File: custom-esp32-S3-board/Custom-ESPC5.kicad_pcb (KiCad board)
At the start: 4 copper layers, 63.5 x 57.1 mm, 43 parts, among them J1 Screw_Terminal_01x02, J10 Barrel_Jack, J12 Conn_01x05, J13 Conn_01x05, J4 USB_C_Receptacle_USB2.0_14P, J5 Conn_01x03, J6 Screw_Terminal_01x03, SW1 SW_Nidec_CAS-120A1, SW2 SW_Push, SW3 SW_Push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

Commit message: Update layout
apply schematic changes to layout
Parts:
- added C10: 10µF, Capacitor_SMD:C_0402_1005Metric, F.Cu at (117.5, 94.0)
- added C11: 0.1uF, Capacitor_SMD:C_0402_1005Metric, F.Cu at (117.5, 96.0)
- added C12: 0.1µF, Capacitor_SMD:C_0402_1005Metric, F.Cu at (117.5, 97.9)
- added C13: 0.1µF, Capacitor_SMD:C_0402_1005Metric, F.Cu at (117.5, 99.9)
- added C15: 10µF, Capacitor_SMD:C_0402_1005Metric, F.Cu at (117.5, 101.9)
- added C16: 0.1µF, Capacitor_SMD:C_0402_1005Metric, F.Cu at (117.5, 103.8)
- added C9: 0.1uF, Capacitor_SMD:C_0402_1005Metric, F.Cu at (117.5, 92.0)
- added R10: 3.3k, Resistor_SMD:R_0402_1005Metric, F.Cu at (120.4, 92.0)
- added R12: 3.3k, Resistor_SMD:R_0402_1005Metric, F.Cu at (120.4, 94.0)
- R1: value 910 -> 750
- U2: value LM317DCYR -> LM317KCS; footprint Package_TO_SOT_SMD:SOT-223-3_TabPin2 -> Package_TO_SOT_THT:TO-220-3_Vertical
- U4: value LM3940 -> LM3940IT-3.3; footprint Package_TO_SOT_SMD:SOT-223-3_TabPin2 -> Package_TO_SOT_THT:TO-220-3_Vertical
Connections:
- U3 pad 6: +3.3V -> CP2102_VDD

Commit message: Fix pin labels in schematic
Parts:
- removed D1, D4: D, Diode_SMD:USC-TOS
- added C17: 0.1u, Capacitor_SMD:C_0402_1005Metric, F.Cu at (125.9, 111.2)
- added C18: 0.1u, Capacitor_SMD:C_0402_1005Metric, F.Cu at (125.9, 113.2)
- added C19: 0.1u, Capacitor_SMD:C_0402_1005Metric, F.Cu at (125.9, 115.1)
- added C20: 0.1u, Capacitor_SMD:C_0402_1005Metric, F.Cu at (125.9, 117.1)
- added J2: Conn_01x02_Pin, Connector_PinHeader_2.54mm:PinHeader_1x02_P2.54mm_Vertical, F.Cu at (126.8, 105.4)
- added J3: Conn_01x02_Pin, Connector_PinHeader_2.54mm:PinHeader_1x02_P2.54mm_Vertical, F.Cu at (131.4, 105.4)
- added J7: Conn_01x02_Pin, Connector_PinHeader_2.54mm:PinHeader_1x02_P2.54mm_Vertical, F.Cu at (136.0, 105.4)
- added J8: Conn_01x02_Pin, Connector_PinHeader_2.54mm:PinHeader_1x02_P2.54mm_Vertical, F.Cu at (140.6, 105.4)
- added Q1: BC847BDW1, Package_TO_SOT_SMD:SOT-363_SC-70-6, F.Cu at (129.7, 112.1)
- added R13: 10k, Resistor_SMD:R_0402_1005Metric, F.Cu at (128.8, 114.8)
- added R14: 10k, Resistor_SMD:R_0402_1005Metric, F.Cu at (128.8, 116.8)
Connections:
- net /UART RX renamed /UART0 RX
- net /UART TX renamed /UART0 TX
- J5 pad 1: +3.3V -> /UART1_TX
- J5 pad 2: /WS2812 -> /UART1_RX
- U6 pad 10: /WS2812 -> /UART1 TX
- U6 pad 11: unconnected-(U6-IO18-Pad11) -> /UART1 RX
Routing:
- net (no net): track 0.00 -> 137.0 mm, vias 0 -> 1
- net /WS2812: track 51.5 -> 0.00 mm, vias 1 -> 0
- net /UART0 RX: track 34.7 -> 0.00 mm
- net /UART0 TX: track 33.7 -> 0.00 mm
- net Net-(J8-Pin_1): track 17.0 -> 0.00 mm

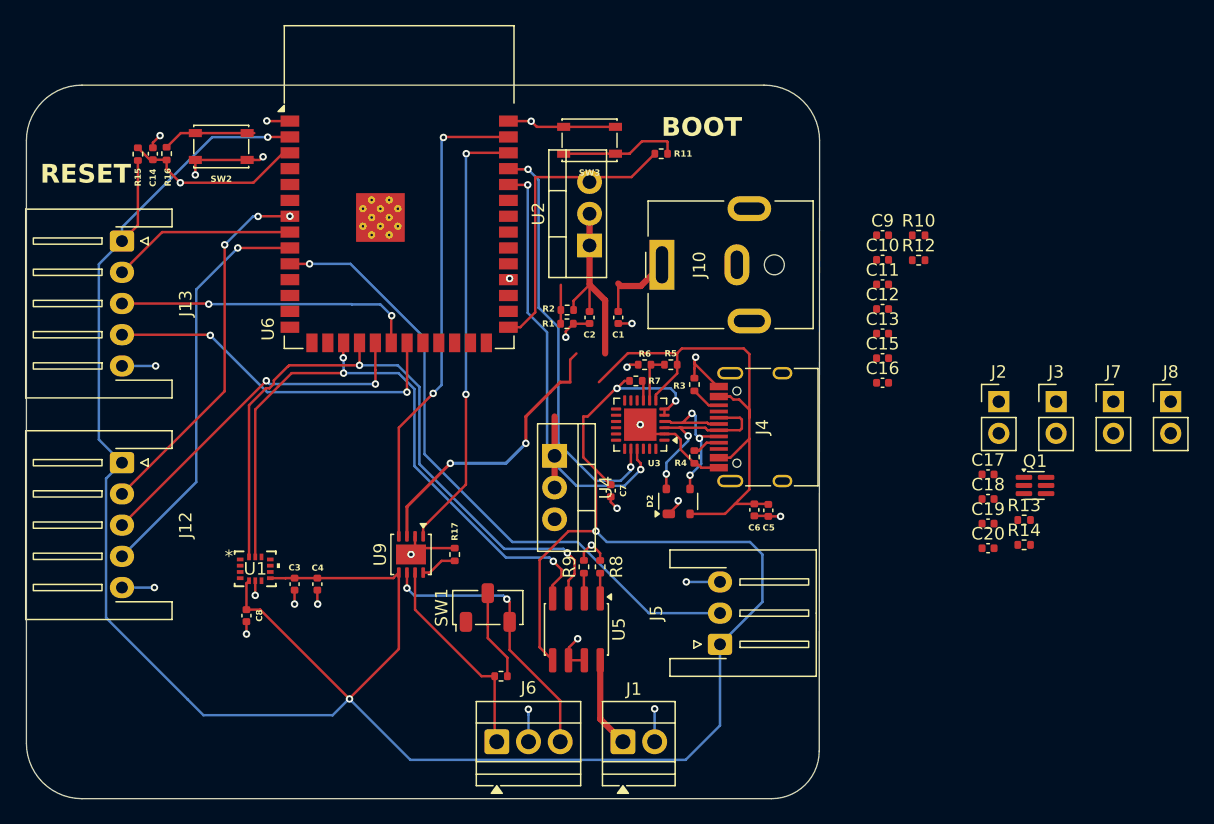
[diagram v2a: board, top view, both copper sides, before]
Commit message: Place components for layout
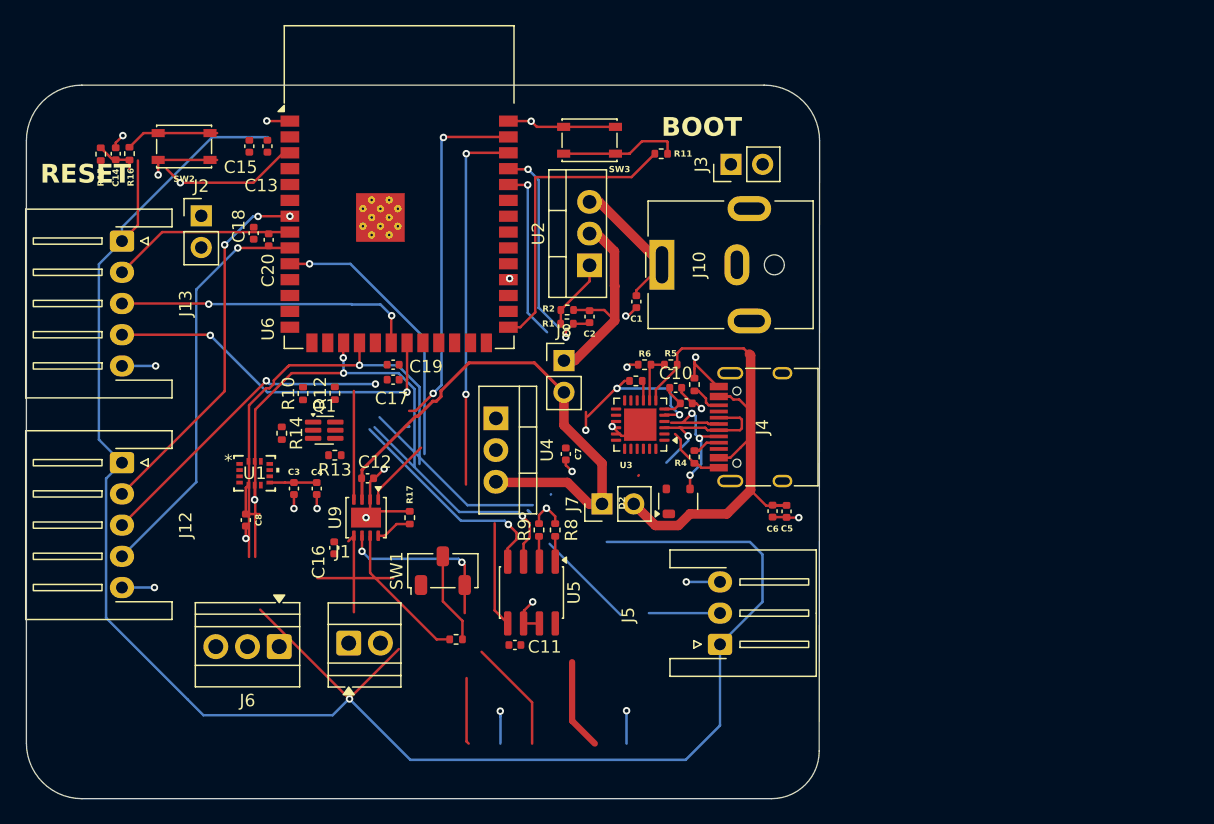
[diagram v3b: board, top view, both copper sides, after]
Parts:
- moved J2 65.6 mm to (62.9, 90.5)
- moved C20 62.7 mm to (68.3, 92.4), turned to -90 degrees
- moved C18 62.6 mm to (67.1, 91.9), turned to -90 degrees
- moved R14 60.1 mm to (69.3, 107.9), turned to -90 degrees
- moved Q1 57.1 mm to (72.8, 107.7)
- moved R13 55.5 mm to (73.6, 109.7), turned to 180 degrees
- moved C15 53.5 mm to (66.8, 84.9), turned to -90 degrees
- moved C13 51.5 mm to (68.2, 84.9), turned to -90 degrees
- moved R10 50.9 mm to (71.0, 104.7), turned to 90 degrees
- moved C19 49.3 mm to (78.3, 102.4)
- moved J8 48.7 mm to (92.0, 102.1)
- moved C17 48.3 mm to (78.3, 103.6)
- moved R12 48.0 mm to (73.6, 104.7), turned to 90 degrees
- moved C16 45.9 mm to (73.5, 117.1), turned to -90 degrees
- moved C12 43.4 mm to (76.2, 111.5)
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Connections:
- J5 pad 1: /UART1_TX -> /UART1 TX
- J5 pad 2: /UART1_RX -> /UART1 RX
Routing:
- net (no net): track 137.0 -> 23.2 mm, vias 1 -> 0
- net /UART1 TX: track 0.00 -> 22.5 mm, vias 0 -> 1
- net +5V: track 23.3 -> 43.4 mm, vias 2 -> 0
- net Net-(J8-Pin_1): track 0.00 -> 17.2 mm
- net +3.3V: track 215.2 -> 198.1 mm, vias 5 -> 4
- net /UART0 TX: track 0.00 -> 15.3 mm, vias 2 -> 1
- net /UART0 RX: track 0.00 -> 14.0 mm, vias 2 -> 1
- net /UART1 RX: track 0.00 -> 5.70 mm
- net Net-(U2-VI): track 6.57 -> 11.2 mm
- net GND: track 76.3 -> 72.8 mm, vias 26 -> 25
- net /A2: track 28.5 -> 25.2 mm
- net CP2102_VDD: track 0.00 -> 3.06 mm
- net Net-(U2-ADJ): track 3.13 -> 5.64 mm
- net Net-(U3-D+): track 15.0 -> 12.8 mm, vias 2 -> 1
- net /CAN RX: track 38.6 -> 37.3 mm

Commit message: Finish routing for subcircuits
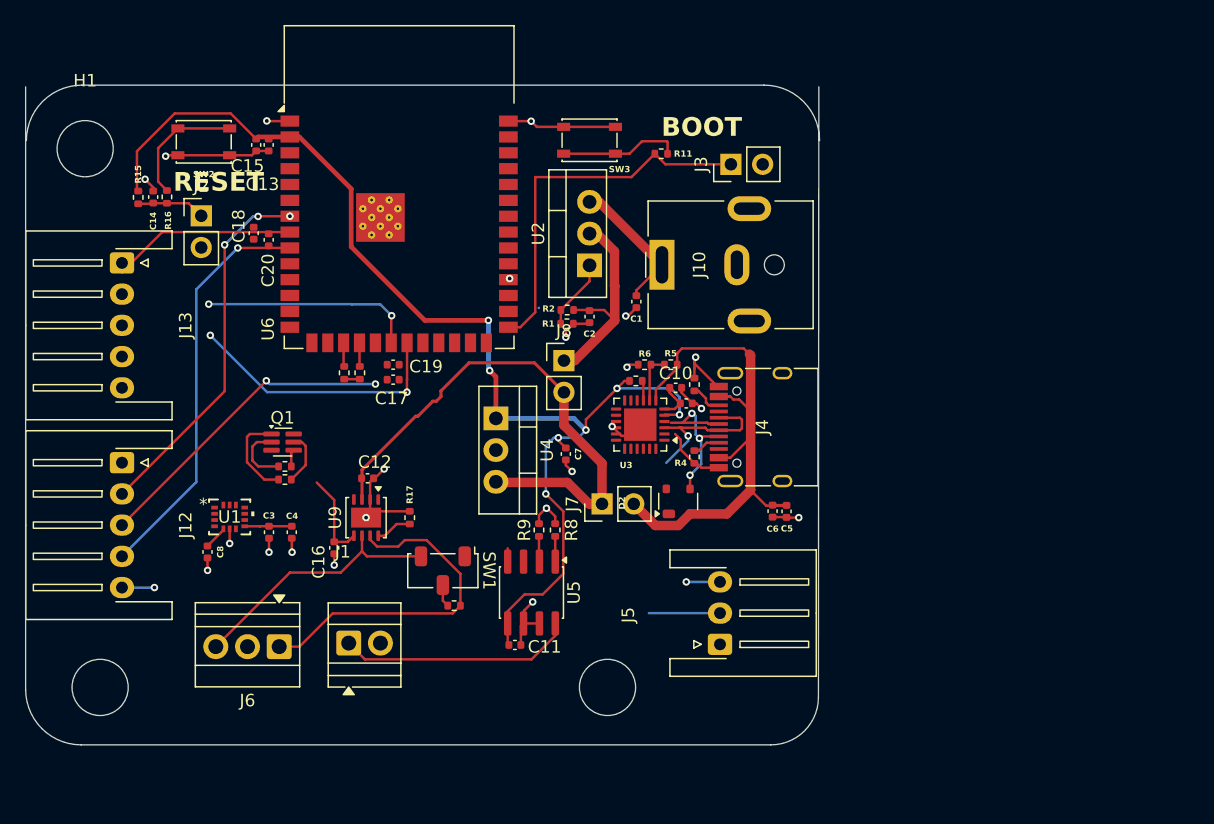
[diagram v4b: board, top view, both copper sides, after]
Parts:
- added H1: MountingHole, MountingHole:MountingHole_4.5mm, F.Cu at (53.6, 85.1)
- added H2: MountingHole, MountingHole:MountingHole_4.5mm, F.Cu at (95.4, 128.2)
- added H3: MountingHole, MountingHole:MountingHole_4.5mm, F.Cu at (54.8, 128.2)
- moved C14 4.58 mm to (59.0, 89.0)
- moved R15 4.58 mm to (57.9, 89.0), turned to -90 degrees
- moved R16 4.58 mm to (60.1, 89.0)
- moved R13 4.10 mm to (69.6, 110.5)
- moved C3 4.03 mm to (68.3, 115.8)
- moved C4 4.03 mm to (70.2, 115.8)
- moved U1 4.03 mm to (65.2, 114.6)
- moved C8 3.99 mm to (63.4, 117.4)
- moved R14 3.72 mm to (69.6, 111.6), turned to 0 degrees
- moved R10 3.69 mm to (74.3, 103.0)
- moved Q1 3.47 mm to (69.4, 108.6)
- moved R18 2.70 mm to (83.2, 121.7), turned to 180 degrees
- moved R12 2.59 mm to (75.6, 103.0)
- moved J13 1.75 mm to (56.5, 94.2)
- moved SW2 1.62 mm to (63.1, 84.5)
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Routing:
- net +3.3V: track 198.1 -> 110.9 mm, vias 4 -> 7
- net /SDA: track 54.9 -> 1.84 mm, vias 2 -> 0
- net /SCL: track 52.7 -> 3.09 mm, vias 3 -> 0
- net /CAN RX: track 37.3 -> 0.00 mm, vias 2 -> 0
- net /CAN TX: track 35.5 -> 0.00 mm, vias 2 -> 0
- net (no net): track 23.2 -> 0.00 mm
- net /UART1 TX: track 22.5 -> 0.01 mm, vias 1 -> 0
- net /UART0 TX: track 15.3 -> 0.10 mm, vias 1 -> 0
- net /UART0 RX: track 14.0 -> 0.04 mm, vias 1 -> 0
- net Net-(J1-Pin_1): track 7.28 -> 18.8 mm
- net Net-(J6-Pin_1): track 16.9 -> 27.5 mm
- net /CHIP_PU: track 14.5 -> 5.50 mm, vias 1 -> 0
- net /UART RTS: track 0.00 -> 7.19 mm
- net /IDX1: track 28.7 -> 21.7 mm
- net /A1: track 24.2 -> 17.3 mm
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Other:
- board size 63.5 x 57.1 mm -> 63.6 x 52.8 mm

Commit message: finished pcb design, left mounting hole still chopped
austin yun 😝😝😝😝😝😝
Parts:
- moved C20 1.07 mm to (67.8, 91.5)
- moved C18 0.77 mm to (66.5, 91.5)
- moved H2 0.50 mm to (94.9, 128.2)
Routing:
- net Net-(J3-Pin_2): track 0.00 -> 60.1 mm, vias 0 -> 5
- net /UART1 TX: track 0.01 -> 57.3 mm, vias 0 -> 1
- net /SDA: track 1.84 -> 53.4 mm, vias 0 -> 3
- net /UART1 RX: track 5.70 -> 53.1 mm, vias 0 -> 1
- net +3.3V: track 110.9 -> 155.7 mm, vias 7 -> 9
- net /UART DTR: track 1.38 -> 45.3 mm, vias 0 -> 2
- net /SCL: track 3.09 -> 42.4 mm, vias 0 -> 3
- net /CAN RX: track 0.00 -> 37.0 mm, vias 0 -> 2
- net /UART0 TX: track 0.10 -> 35.4 mm, vias 0 -> 2
- net /UART0 RX: track 0.04 -> 35.0 mm, vias 0 -> 2
- net /UART RTS: track 7.19 -> 40.2 mm, vias 0 -> 2
- net /CAN TX: track 0.00 -> 32.8 mm, vias 0 -> 2
- net Net-(J2-Pin_2): track 0.00 -> 30.0 mm, vias 0 -> 2
- net GND: track 70.7 -> 99.3 mm, vias 23 -> 27
- net /CHIP_PU: track 5.50 -> 16.0 mm
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
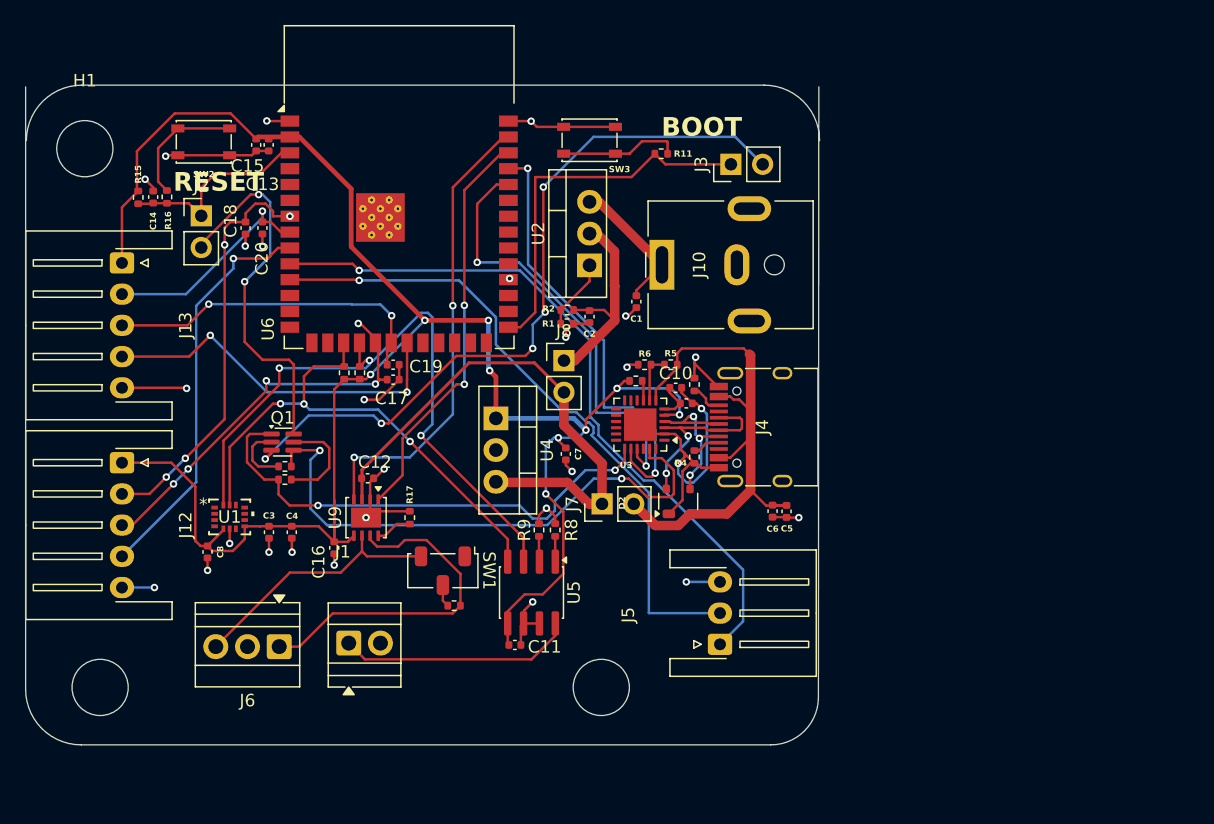
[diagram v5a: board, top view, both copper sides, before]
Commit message: Fix board outline
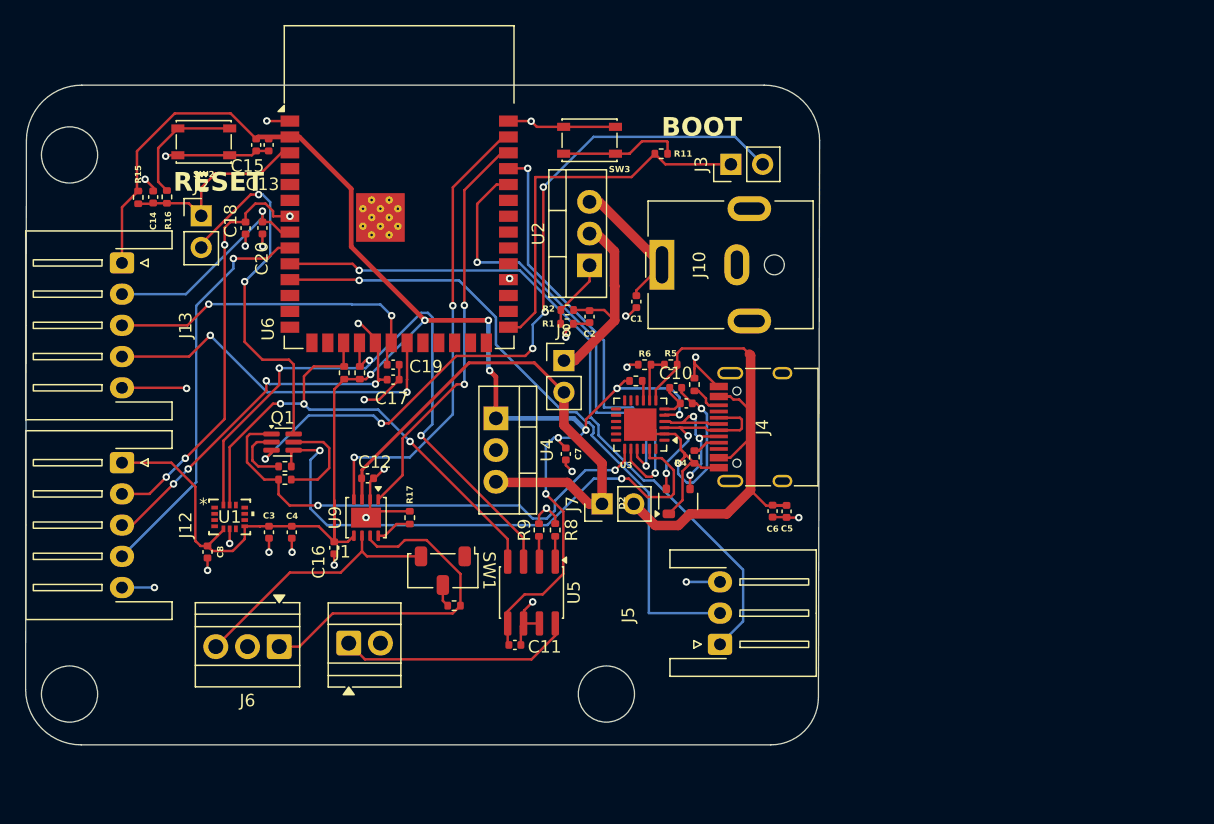
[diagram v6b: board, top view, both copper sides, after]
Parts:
- moved H3 2.51 mm to (52.4, 128.8)
- moved H1 1.32 mm to (52.4, 85.6)
- moved H2 0.67 mm to (95.3, 128.8)
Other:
- outline, holes or cut-outs redrawn
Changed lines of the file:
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@@
 	(footprint "MountingHole:MountingHole_4.5mm"
 		(layer "F.Cu")
-		(at 53.575 85.1)
+		(at 52.35 85.6)
 		(descr "Mounting Hole 4.5mm, no annular, generated by kicad-footprint-generator mountinghole.py")
 		(tags "mountinghole")
@@
 			(at 0 -5.45 0)
 			(layer "F.SilkS")
+			(hide yes)
 			(effects
 				(font
@@
 	(footprint "MountingHole:MountingHole_4.5mm"
 		(layer "F.Cu")
-		(at 94.94 128.25)
+		(at 95.35 128.78)
 		(descr "Mounting Hole 4.5mm, no annular, generated by kicad-footprint-generator mountinghole.py")
 		(tags "mountinghole")
@@
 	(footprint "MountingHole:MountingHole_4.5mm"
 		(layer "F.Cu")
-		(at 54.8 128.25)
+		(at 52.35 128.78)
 		(descr "Mounting Hole 4.5mm, no annular, generated by kicad-footprint-generator mountinghole.py")
 		(tags "mountinghole")
@@
 	)
 	(gr_line
-		(start 112.36441 80.145)
+		(start 112.4269 84.455)
 		(end 112.3325 129.04)
 		(stroke
@@
 		(layer "Edge.Cuts")
 	)
-	(gr_line
-		(start 48.8325 80.145)
-		(end 48.8325 128.405)
-		(stroke
-			(width 0.05)
-			(type default)
-		)
-		(layer "Edge.Cuts")
-	)
 	(gr_arc
 		(start 107.98191 80.01)
@@
 		(end 48.8325 128.405)
 		(stroke
+			(width 0.05)
+			(type default)
+		)
+		(layer "Edge.Cuts")
+	)
+	(gr_line
+		(start 48.895 84.455)
+		(end 48.8325 128.405)
+		(stroke

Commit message: did some silkscreen labeling
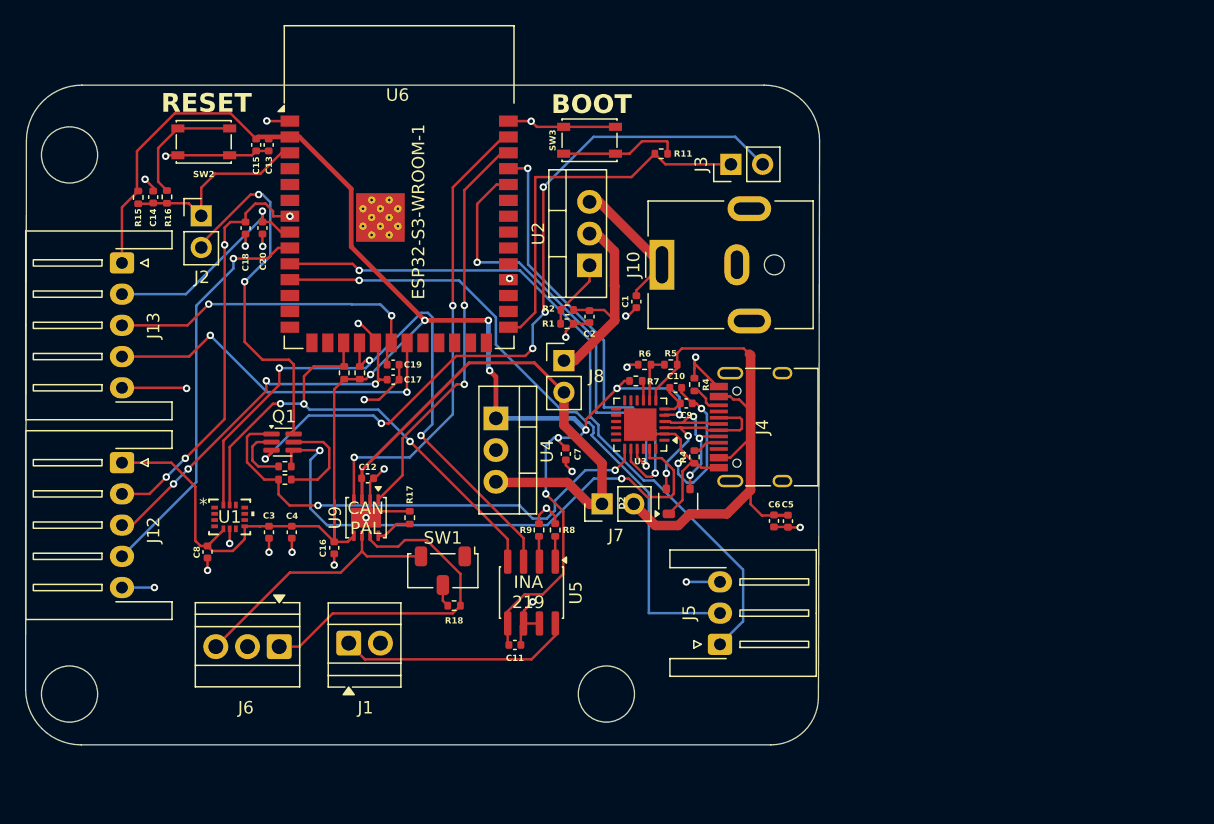
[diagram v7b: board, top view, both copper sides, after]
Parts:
- moved C6 0.79 mm to (108.8, 114.9)
- moved C5 0.79 mm to (109.9, 114.9)
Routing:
- net Net-(J7-Pin_2): track 43.3 -> 44.4 mm
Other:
- board text added: "C9"
- board text added: "CAN PAL"
- board text added: "ESP32-S3-WROOM-1"
- board text added: "INA 219"
- board text added: "R18"
- board text added: "R4"
- board text added: "R7"

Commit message: more labeling
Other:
- board text added: "+"
- board text added: "-"
- board text added: "120 Ω"
- board text added: "15V PDP IN"
- board text added: "3.3V"
- board text added: "April 20th, 2026"
- board text added: "CAN"
- board text added: "CANH"
- board text added: "CANL"
- board text added: "CHIP PU"
- board text added: "ENCB"
- board text added: "ENCF"
- board text added: "ESP Quack S3 DevBoard"
- board text added: "GND"
- board text added: "IMU"
- board text added: "PDH PWR SEL"
- board text added: "RX"
- board text added: "Roger Zhu Austen Yun"
- board text added: "SCL"
- board text added: "TX"
- board text added: "UART"
- board text added: "USB PWR SEL"
- board text added: "VSense"
- board text removed: "C9"
- board text removed: "CAN PAL"
- board text removed: "ESP32-S3-WROOM-1"
- board text removed: "INA 219"
- board text removed: "R4"
- board text removed: "R7"
